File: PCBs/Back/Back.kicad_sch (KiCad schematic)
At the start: 137 parts, among them J1 TC2030, U2 Ch32v003F4U6

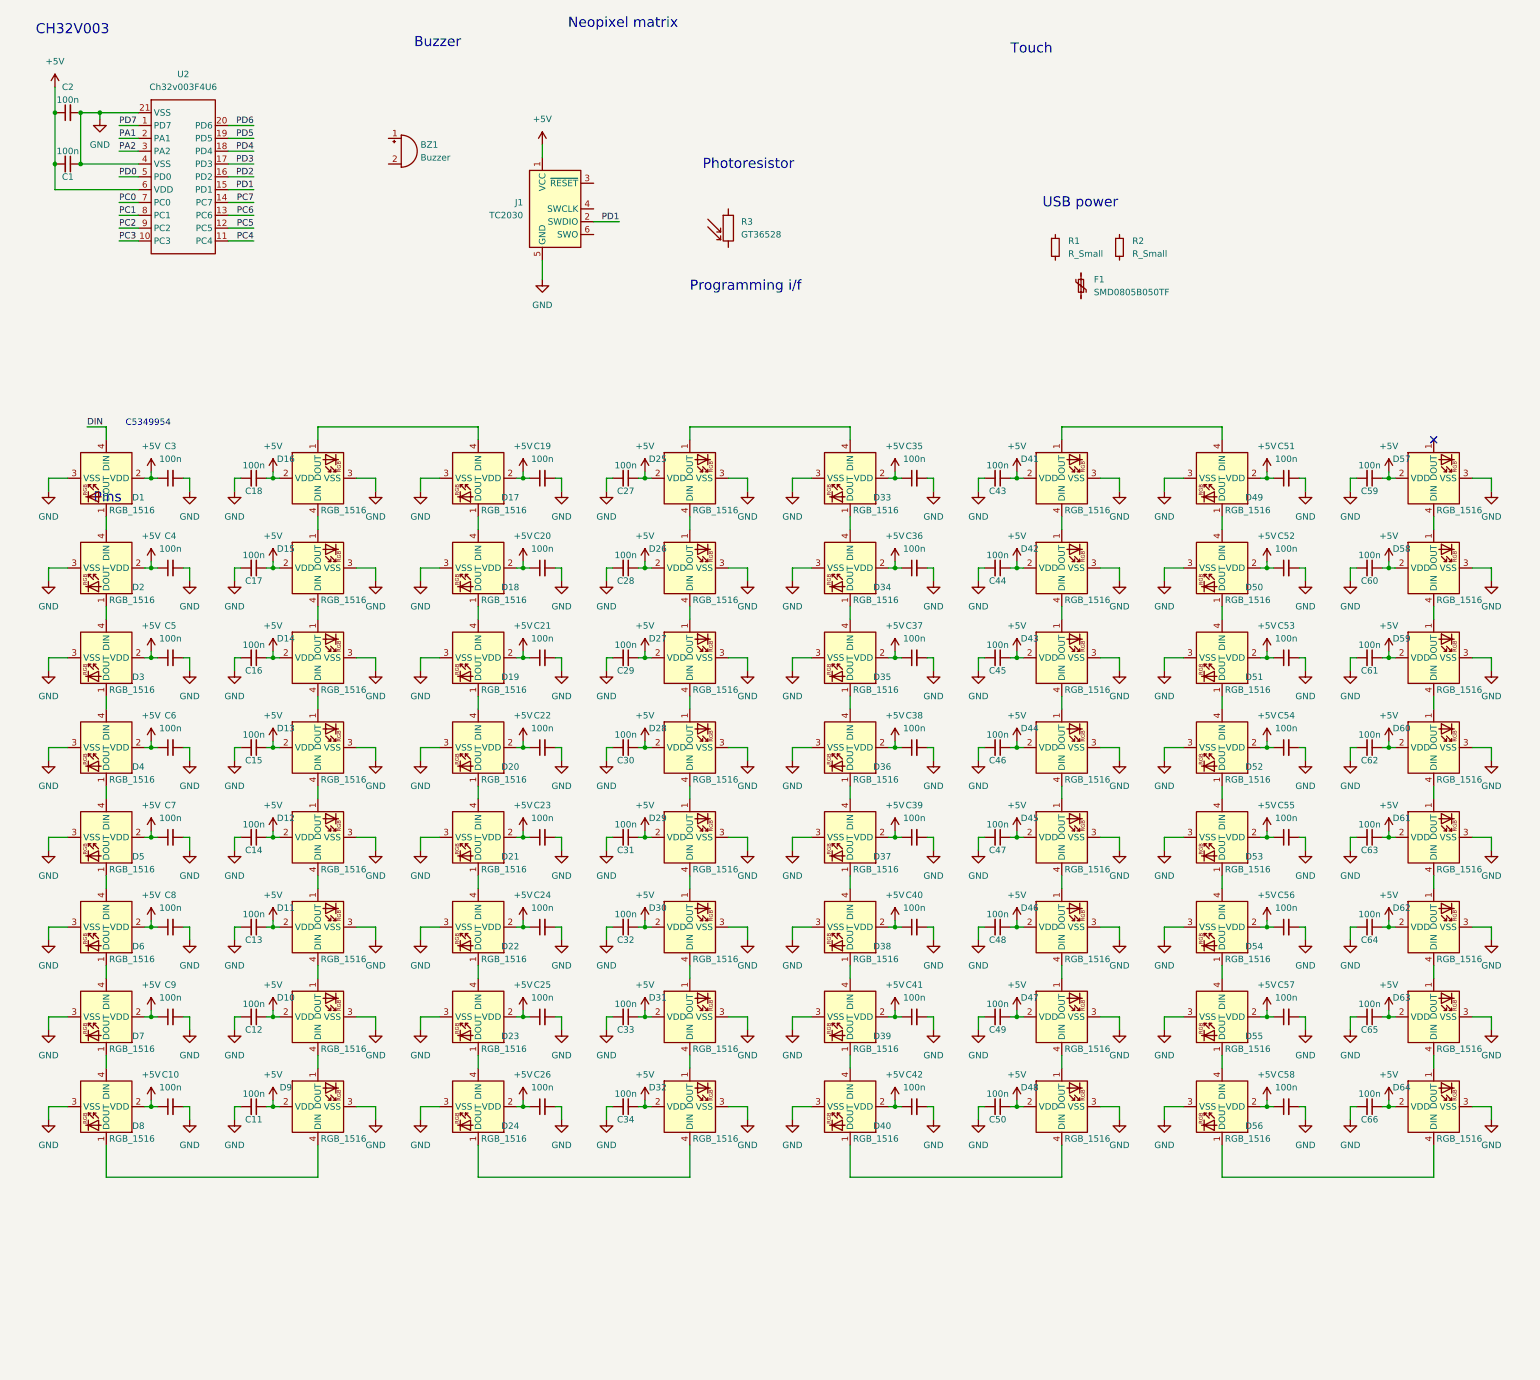
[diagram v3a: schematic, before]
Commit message: Updated back schematic
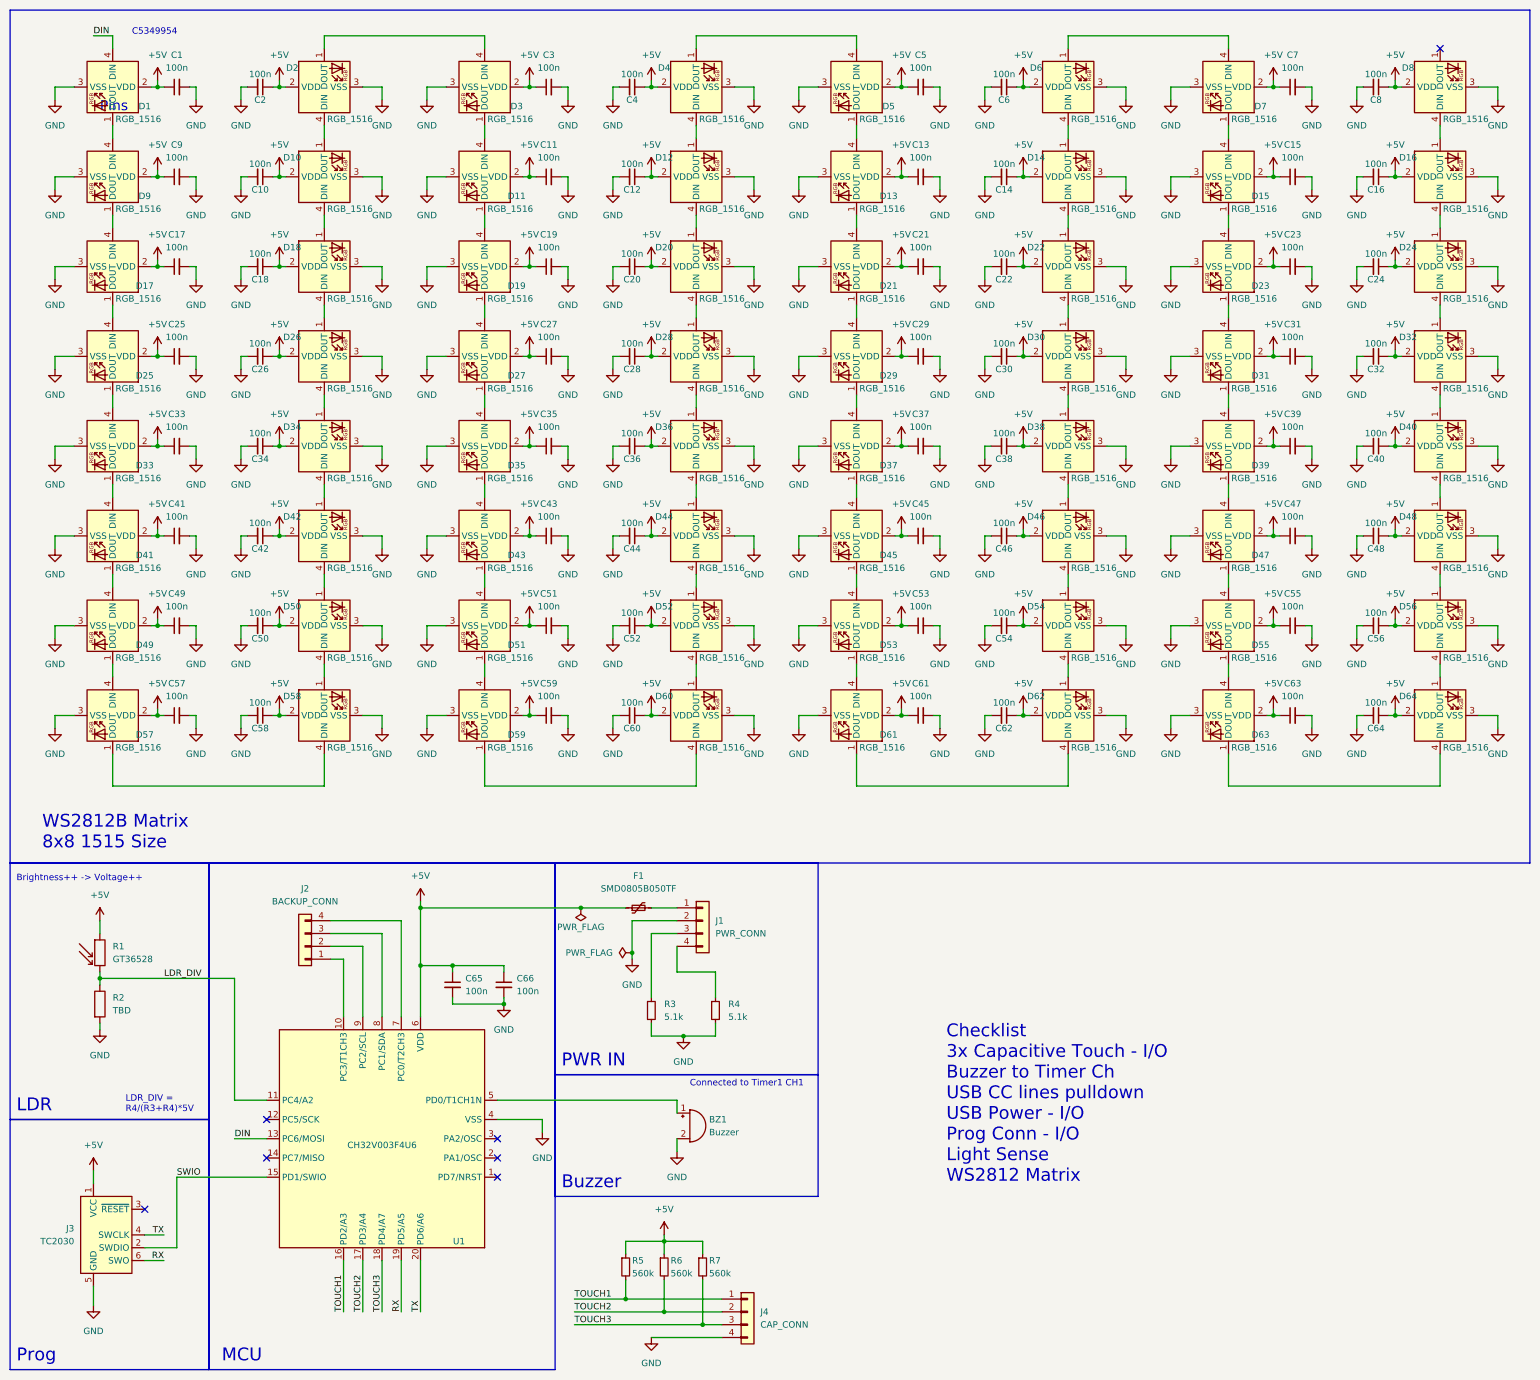
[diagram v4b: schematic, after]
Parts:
- removed C1, C2: 100n, symbol Device:C_Small
- removed U2: Ch32v003F4U6, Package_DFN_QFN:QFN-20-1EP_3x3mm_P0.4mm_EP1.65x1.65mm, symbol Back-lib:Ch32v003F4U6
- added C65, C66: 100n, symbol Device:C_Small
- added J1: PWR_CONN, symbol Connector_Generic:Conn_01x04
- added J2: BACKUP_CONN, symbol Connector_Generic:Conn_01x04
- added J4: CAP_CONN, symbol Connector_Generic:Conn_01x04
- added R2: TBD, symbol Device:R
- added R5, R6, R7: 560k, symbol Device:R_Small
- added U1: CH32V003F4U6, Package_DFN_QFN:QFN-20-1EP_3x3mm_P0.4mm_EP1.65x1.65mm, symbol Back-lib:CH32V003F4U6
- R3: renamed from R1; value R_Small -> 5.1k
- R4: renamed from R2; value R_Small -> 5.1k
- renumbered C3 to C1, C17 to C10, C20 to C11, C28 to C12, C36 to C13, C44 to C14, C52 to C15, C60 to C16, C5 to C17, C16 to C18, C21 to C19, C18 to C2, C29 to C20, C37 to C21, C45 to C22, C53 to C23, C61 to C24, C6 to C25, C15 to C26, C22 to C27, C30 to C28, C38 to C29, C19 to C3, C46 to C30, C54 to C31, C62 to C32, C7 to C33, C14 to C34, C23 to C35, C31 to C36, C39 to C37, C47 to C38, C55 to C39, C27 to C4, C63 to C40, C8 to C41, C13 to C42, C24 to C43, C32 to C44, C40 to C45, C48 to C46, C56 to C47, C64 to C48, C9 to C49, C35 to C5, C12 to C50, C25 to C51, C33 to C52, C41 to C53, C49 to C54, C57 to C55, C65 to C56, C10 to C57, C11 to C58, C26 to C59, C43 to C6, C34 to C60, C42 to C61, C50 to C62, C58 to C63, C66 to C64, C51 to C7, C59 to C8, C4 to C9, D15 to D10, D18 to D11, D26 to D12, D34 to D13, D42 to D14, D50 to D15, D58 to D16, D3 to D17, D14 to D18, D16 to D2, D27 to D20, D35 to D21, D43 to D22, D51 to D23, D59 to D24, D4 to D25, D13 to D26, D20 to D27, D36 to D29, D17 to D3, D44 to D30, D52 to D31, D60 to D32, D5 to D33, D12 to D34, D21 to D35, D29 to D36, D45 to D38, D53 to D39, D25 to D4, D61 to D40, D6 to D41, D11 to D42, D22 to D43, D30 to D44, D38 to D45, D54 to D47, D62 to D48, D7 to D49, D33 to D5, D10 to D50, D23 to D51, D31 to D52, D39 to D53, D47 to D54, D63 to D56, D8 to D57, D9 to D58, D24 to D59, D41 to D6, D32 to D60, D40 to D61, D48 to D62, D56 to D63, D49 to D7, D57 to D8, D2 to D9, J1 to J3, R3 to R1
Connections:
- net +5V: now also F1.1, R1.1, C65.1, C66.1, R5.1, R6.1, R7.1, U1.6 (VDD)
- net DIN: now also U1.13 (PC6/MOSI)
- net GND: now also BZ1.2 (+), R3.2, R4.2, C65.2, C66.2, J1.2 (Pin_2), J4.4 (Pin_4), R2.2, U1.21 (VSS), U1.4 (VSS)
- net LDR_DIV: now reaches R1.2
- net LDR_DIV: now also R2.1, U1.11 (PC4/A2)
- net at R3.1: now also J1.3 (Pin_3)
- net at R4.1: now also J1.4 (Pin_4)
- net at BZ1.1 (-): now also U1.5 (PD0/T1CH1N)
- net TX: now reaches J3.4 (SWCLK)
- net TX: now also U1.20 (PD6/A6)
- net RX: now reaches J3.6 (SWO)
- net RX: now also U1.19 (PD5/A5)
- net at F1.2: now also J1.1 (Pin_1)
- net PD1 renamed SWIO
- net SWIO: now also U1.15 (PD1/SWIO)
- new net: J2.1 (Pin_1), U1.10 (PC3/T1CH3)
- new net: J2.4 (Pin_4), U1.7 (PC0/T2CH3)
- new net: J2.3 (Pin_3), U1.8 (PC1/SDA)
- new net: J2.2 (Pin_2), U1.9 (PC2/SCL)
- new net TOUCH1: J4.1 (Pin_1), R5.2, U1.16 (PD2/A3)
- new net TOUCH2: J4.2 (Pin_2), R6.2, U1.17 (PD3/A4)
- new net TOUCH3: J4.3 (Pin_3), R7.2, U1.18 (PD4/A7)
- no-connect marks 1 -> 7
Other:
- note added: "Brightness++ -> Voltage++"
- note added: "Checklist 3x Capacitive Touch - I/O Buzzer to Timer Ch USB CC lines pulldown USB Power - I/O Prog Conn - I/O Light Sense WS2812 Matrix"
- note added: "Connected to Timer1 CH1"
- note added: "LDR"
- note added: "LDR_DIV = R4/(R3+R4)*5V"
- note added: "MCU"
- note added: "PWR IN"
- note added: "Prog"
- note added: "WS2812B Matrix 8x8 1515 Size"
- note removed: "CH32V003"
- note removed: "Neopixel matrix"
- note removed: "Photoresistor"
- note removed: "Programming i/f"
- note removed: "Touch"
- note removed: "USB power"
- moved on the sheet: BZ1, C1, C10, C11, C12, C13, C14, C15, C16, C17, C18, C19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

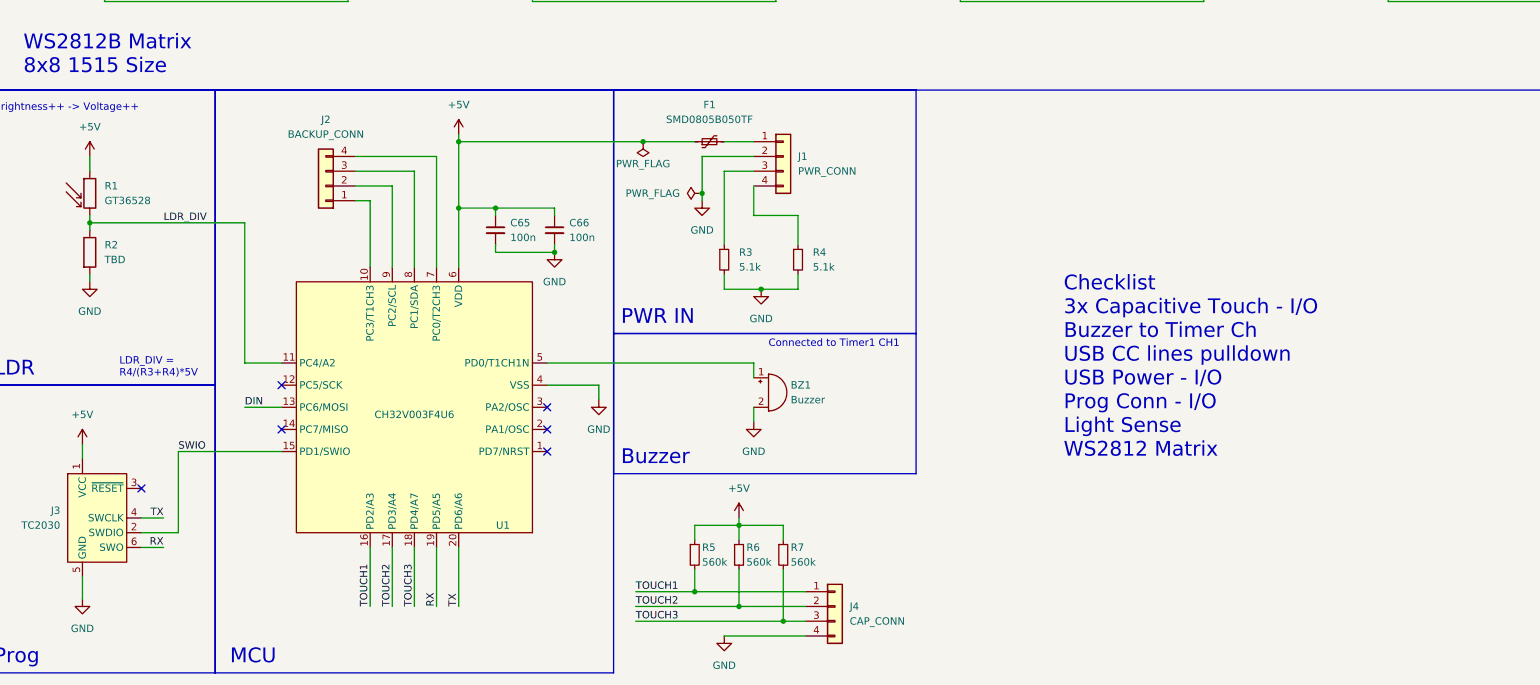
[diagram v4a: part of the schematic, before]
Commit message: Back schematic finished
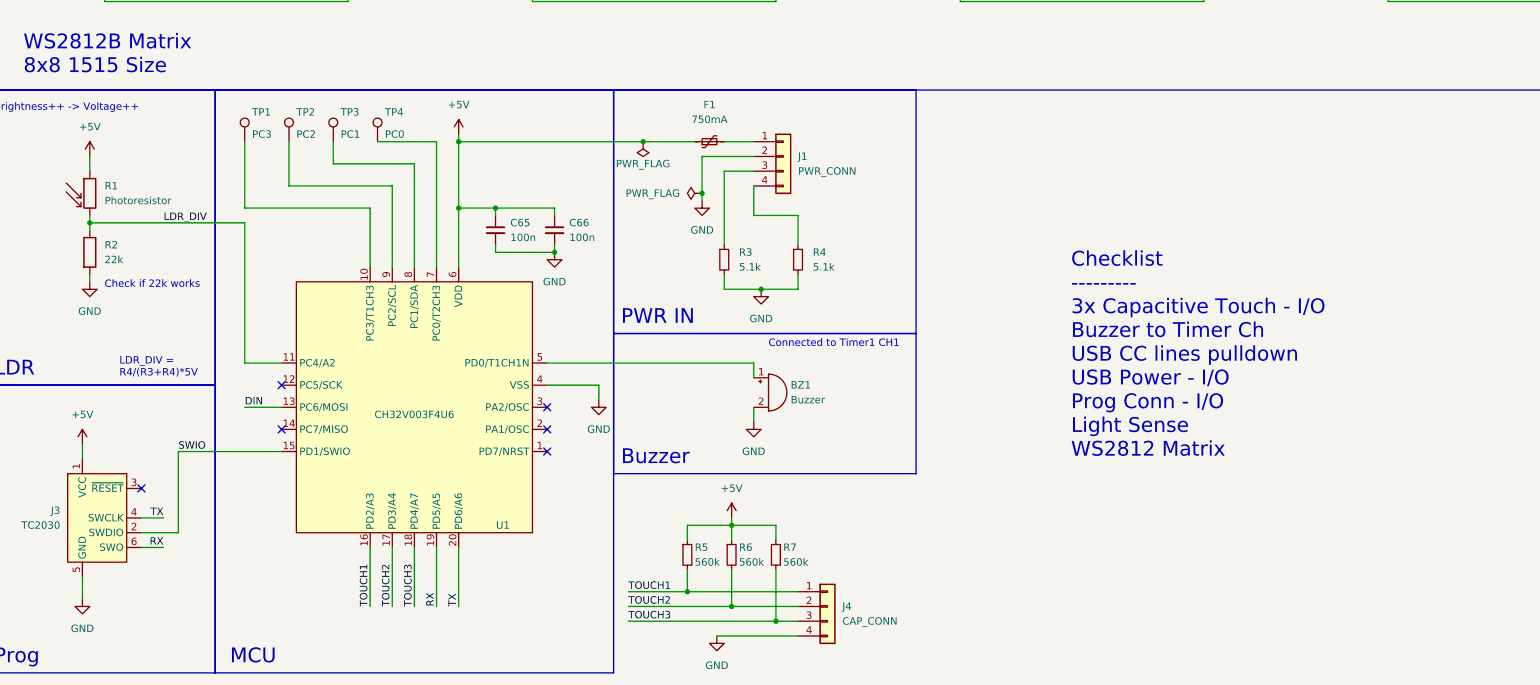
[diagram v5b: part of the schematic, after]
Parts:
- removed J2: BACKUP_CONN, symbol Connector_Generic:Conn_01x04
- added TP1: PC3, TestPoint:TestPoint_Pad_D2.0mm, symbol Connector:TestPoint
- added TP2: PC2, TestPoint:TestPoint_Pad_D2.0mm, symbol Connector:TestPoint
- added TP3: PC1, TestPoint:TestPoint_Pad_D2.0mm, symbol Connector:TestPoint
- added TP4: PC0, TestPoint:TestPoint_Pad_D2.0mm, symbol Connector:TestPoint
- BZ1: footprint (none) -> fp:FUET-1325; LCSC (none) -> C391038
- C1, C10, C11, C12, C13, C14, C15, C16, C17, C18, C19, C2, C20, C21, C22, C23, C24, C25, C26, C27, C28, C29, C3, C30, C31, C32, C33, C34, C35, C36, C37, C38, C39, C4, C40, C41, C42, C43, C44, C45, C46, C47, C48, C49, C5, C50, C51, C52, C53, C54, C55, C56, C57, C58, C59, C6, C60, C61, C62, C63, C64, C65, C66, C7, C8, C9: footprint (none) -> Capacitor_SMD:C_0402_1005Metric; LCSC (none) -> C1525
- D1, D10, D11, D12, D13, D14, D15, D16, D17, D18, D19, D2, D20, D21, D22, D23, D24, D25, D26, D27, D28, D29, D3, D30, D31, D32, D33, D34, D35, D36, D37, D38, D39, D4, D40, D41, D42, D43, D44, D45, D46, D47, D48, D49, D5, D50, D51, D52, D53, D54, D55, D56, D57, D58, D59, D6, D60, D61, D62, D63, D64, D7, D8, D9: footprint fp:WS2812B_1515 -> fp:XL-1615_WS2812B; LCSC (none) -> C5349954
- F1: value SMD0805B050TF -> 750mA; LCSC (none) -> C269105
- J1, J4: footprint (none) -> Connector_PinHeader_2.54mm:PinHeader_1x04_P2.54mm_Vertical
- R1: value GT36528 -> Photoresistor; footprint (none) -> fp:GT36528; LCSC (none) -> C2904881
- R2: value TBD -> 22k; footprint (none) -> Resistor_SMD:R_0603_1608Metric; LCSC (none) -> C31850
- R3, R4: footprint (none) -> Resistor_SMD:R_0603_1608Metric; LCSC (none) -> C23186
- R5, R6, R7: footprint (none) -> Resistor_SMD:R_0603_1608Metric; LCSC (none) -> C23203
- U1: LCSC (none) -> C5299908
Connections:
- net at U1.10 (PC3/T1CH3): now also TP1.1
- net at U1.7 (PC0/T2CH3): now also TP4.1
- net at U1.8 (PC1/SDA): now also TP3.1
- net at U1.9 (PC2/SCL): now also TP2.1
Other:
- note added: "Check if 22k works"
- note added: "Checklist --------- 3x Capacitive Touch - I/O Buzzer to Timer Ch USB CC lines pulldown USB Power - I/O Prog Conn - I/O Light Sense WS2812 Matrix"
- note removed: "Checklist 3x Capacitive Touch - I/O Buzzer to Timer Ch USB CC lines pulldown USB Power - I/O Prog Conn - I/O Light Sense WS2812 Matrix"
- moved on the sheet: J4, R5, R6, R7

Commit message: back layout done
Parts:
- removed TP4: PC0, TestPoint:TestPoint_Pad_D2.0mm, symbol Connector:TestPoint
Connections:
- net DIN: now also U1.5 (PD0/T1CH1N); no longer U1.13 (PC6/MOSI)
- net RX: now also J3.4 (SWCLK); no longer J3.6 (SWO)
- net TX: now also J3.6 (SWO); no longer J3.4 (SWCLK)
- net BUZ: now reaches BZ1.1 (-)
- net BUZ: now also U1.7 (PC0/T2CH3); no longer U1.5 (PD0/T1CH1N)
- no-connect marks 7 -> 8
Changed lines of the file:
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@@
   (no_connect (at 109.22 238.76))
   (no_connect (at 63.5 234.95))
+  (no_connect (at 63.5 238.76))
   (no_connect (at 39.37 252.73))
   (no_connect (at 109.22 242.57))
@@
     (stroke (width 0) (type default))
   )
+  (wire (pts (xy 134.62 231.14) (xy 144.78 231.14))
+    (stroke (width 0) (type default))
+  )
   (wire (pts (xy 93.98 204.47) (xy 100.33 204.47))
     (stroke (width 0) (type default))
@@
     (stroke (width 0) (type default))
   )
+  (wire (pts (xy 90.17 193.04) (xy 90.17 214.63))
+    (stroke (width 0) (type default))
+  )
   (wire (pts (xy 114.3 101.6) (xy 115.57 101.6))
     (stroke (width 0) (type default))
@@
     (stroke (width 0) (type default))
   )
+  (wire (pts (xy 86.36 193.04) (xy 90.17 193.04))
+    (stroke (width 0) (type default))
+  )
   (wire (pts (xy 180.34 73.66) (xy 180.34 76.2))
     (stroke (width 0) (type default))
@@
     (stroke (width 0) (type default))
   )
-  (wire (pts (xy 109.22 231.14) (xy 144.78 231.14))
-    (stroke (width 0) (type default))
-  )
   (wire (pts (xy 254 127) (xy 254 129.54))
     (stroke (width 0) (type default))
@@
     (stroke (width 0) (type default))
   )
-  (wire (pts (xy 39.37 262.89) (xy 43.18 262.89))
+  (wire (pts (xy 39.37 257.81) (xy 43.18 257.81))
     (stroke (width 0) (type default))
   )
@@
     (stroke (width 0) (type default))
   )
+  (wire (pts (xy 109.22 231.14) (xy 114.3 231.14))
+    (stroke (width 0) (type default))
+  )
   (wire (pts (xy 287.02 154.94) (xy 285.75 154.94))
     (stroke (width 0) (type default))
@@
     (stroke (width 0) (type default))
   )
-  (wire (pts (xy 90.17 193.04) (xy 80.01 193.04))
-    (stroke (width 0) (type default))
-  )
   (wire (pts (xy 139.7 101.6) (xy 138.43 101.6))
     (stroke (width 0) (type default))
@@
     (stroke (width 0) (type default))
   )
-  (wire (pts (xy 57.15 238.76) (xy 63.5 238.76))
-    (stroke (width 0) (type default))
-  )
   (wire (pts (xy 64.77 200.66) (xy 64.77 193.04))
     (stroke (width 0) (type default))
@@
     (stroke (width 0) (type default))
   )
-  (wire (pts (xy 90.17 193.04) (xy 90.17 214.63))
-    (stroke (width 0) (type default))
-  )
   (wire (pts (xy 66.04 137.16) (xy 64.77 137.16))
     (stroke (width 0) (type default))
@@
     (stroke (width 0) (type default))
   )
-  (wire (pts (xy 39.37 257.81) (xy 43.18 257.81))
+  (wire (pts (xy 39.37 262.89) (xy 43.18 262.89))
     (stroke (width 0) (type default))
   )
@@
     (effects (font (size 1.27 1.27)) (justify left bottom))
   )
-  (label "RX" (at 43.18 262.89 180) (fields_autoplaced)
+  (label "RX" (at 43.18 257.81 180) (fields_autoplaced)
     (effects (font (size 1.27 1.27)) (justify right bottom))
   )
-  (label "DIN" (at 57.15 238.76 0) (fields_autoplaced)
+  (label "BUZ" (at 86.36 193.04 0) (fields_autoplaced)
     (effects (font (size 1.27 1.27)) (justify left bottom))
   )
@@
     (effects (font (size 1.27 1.27)) (justify left bottom))
   )
-  (label "TX" (at 43.18 257.81 180) (fields_autoplaced)
+  (label "TX" (at 43.18 262.89 180) (fields_autoplaced)
     (effects (font (size 1.27 1.27)) (justify right bottom))
   )
@@
     (effects (font (size 1.27 1.27)) (justify left bottom))
   )
+  (label "BUZ" (at 134.62 231.14 0) (fields_autoplaced)
+    (effects (font (size 1.27 1.27)) (justify left bottom))
+  )
   (label "TOUCH2" (at 123.19 273.05 0) (fields_autoplaced)
     (effects (font (size 1.27 1.27)) (justify left bottom))
@@
     (effects (font (size 1.27 1.27)) (justify left bottom))
   )
+  (label "DIN" (at 114.3 231.14 180) (fields_autoplaced)
+    (effects (font (size 1.27 1.27)) (justify right bottom))
+  )
   (label "SWIO" (at 45.72 246.38 0) (fields_autoplaced)
     (effects (font (size 1.27 1.27)) (justify left bottom))
@@
         )
       )
-    )
-  )
-  (symbol (lib_id "Connector:TestPoint") (at 80.01 193.04 0) (unit 1)
-    (in_bom yes) (on_board yes) (dnp no)
-    (property "Reference" "TP4" (at 81.28 187.96 0)
-      (effects (font (size 1.27 1.27)) (justify left))
-    )
-    (property "Value" "PC0" (at 81.28 191.77 0)
-      (effects (font (size 1.27 1.27)) (justify left))
-    )
-    (property "Footprint" "TestPoint:TestPoint_Pad_D2.0mm" (at 85.09 193.04 0)
-      (effects (font (size 1.27 1.27)) hide)
-    )
-    (property "Datasheet" "~" (at 85.09 193.04 0)
-      (effects (font (size 1.27 1.27)) hide)
-    )
-    (pin "1")
-    (instances
-      (project "Back"
-        (path "/72978c88-1735-4670-89a5-fb7212a78e0c"
-          (reference "TP4") (unit 1)
-        )
-      )
